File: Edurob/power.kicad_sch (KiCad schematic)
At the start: 26 parts, among them U2 AZ1117-3.3

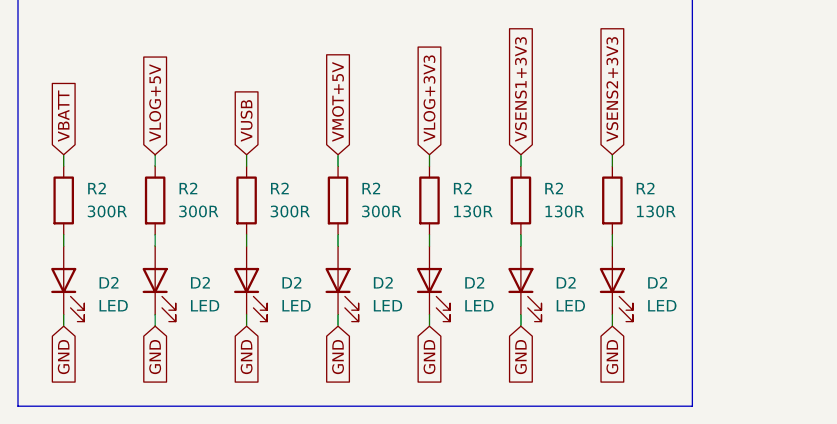
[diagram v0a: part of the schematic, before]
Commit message: Added GPIO Expander, finalized Connector positions
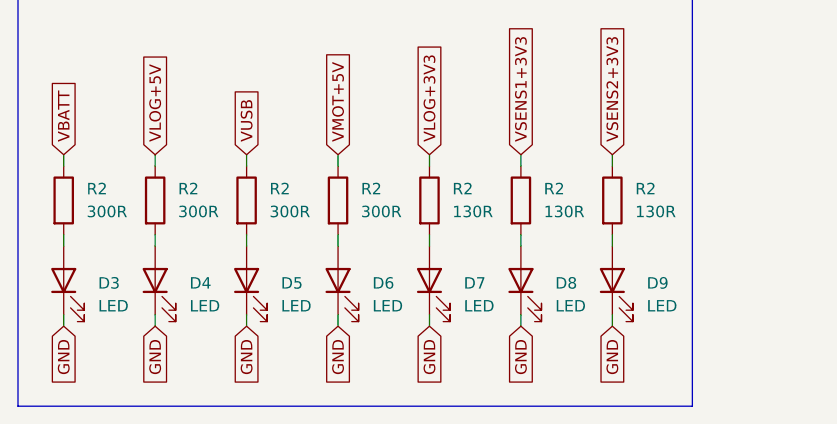
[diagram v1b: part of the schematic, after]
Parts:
- renumbered D2 to D3, D2 to D4, D2 to D5, D2 to D6, D2 to D7, D2 to D8, D2 to D9
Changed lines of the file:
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@@
       )
       (project "Edurob"
-        (path "/ea495553-3cd2-4380-af57-b7ab16ec3dc9"
-          (reference "R1") (unit 1)
-        )
-        (path "/ea495553-3cd2-4380-af57-b7ab16ec3dc9/8aa2f8b0-d8d3-42d6-a936-678d5127e1c2"
-          (reference "R4") (unit 1)
-        )
-        (path "/ea495553-3cd2-4380-af57-b7ab16ec3dc9/172d60ec-c5c3-4534-881f-0378b6cc8d8f"
-          (reference "R6") (unit 1)
-        )
-        (path "/ea495553-3cd2-4380-af57-b7ab16ec3dc9/b565ef5e-ebd0-4632-9832-ca713cd7c533"
-          (reference "R25") (unit 1)
-        )
         (path "/ea495553-3cd2-4380-af57-b7ab16ec3dc9/3d6529d3-09ba-43bd-8600-e24f0f302957"
           (reference "R30") (unit 1)
@@
   (symbol (lib_id "Device:LED") (at 38.1 95.25 90) (unit 1)
     (in_bom yes) (on_board yes) (dnp no) (fields_autoplaced)
-    (property "Reference" "D2" (at 41.91 95.5675 90)
+    (property "Reference" "D5" (at 41.91 95.5675 90)
       (effects (font (size 1.27 1.27)) (justify right))
     )
@@
     (instances
       (project "Edurob"
-        (path "/ea495553-3cd2-4380-af57-b7ab16ec3dc9/b565ef5e-ebd0-4632-9832-ca713cd7c533"
-          (reference "D2") (unit 1)
-        )
         (path "/ea495553-3cd2-4380-af57-b7ab16ec3dc9/3d6529d3-09ba-43bd-8600-e24f0f302957"
           (reference "D5") (unit 1)
@@
   (symbol (lib_id "Device:LED") (at 68.58 95.25 90) (unit 1)
     (in_bom yes) (on_board yes) (dnp no) (fields_autoplaced)
-    (property "Reference" "D2" (at 72.39 95.5675 90)
+    (property "Reference" "D8" (at 72.39 95.5675 90)
       (effects (font (size 1.27 1.27)) (justify right))
     )
@@
     (instances
       (project "Edurob"
-        (path "/ea495553-3cd2-4380-af57-b7ab16ec3dc9/b565ef5e-ebd0-4632-9832-ca713cd7c533"
-          (reference "D2") (unit 1)
-        )
         (path "/ea495553-3cd2-4380-af57-b7ab16ec3dc9/3d6529d3-09ba-43bd-8600-e24f0f302957"
           (reference "D8") (unit 1)
@@
   (symbol (lib_id "Device:LED") (at 58.42 95.25 90) (unit 1)
     (in_bom yes) (on_board yes) (dnp no) (fields_autoplaced)
-    (property "Reference" "D2" (at 62.23 95.5675 90)
+    (property "Reference" "D7" (at 62.23 95.5675 90)
       (effects (font (size 1.27 1.27)) (justify right))
     )
@@
     (instances
       (project "Edurob"
-        (path "/ea495553-3cd2-4380-af57-b7ab16ec3dc9/b565ef5e-ebd0-4632-9832-ca713cd7c533"
-          (reference "D2") (unit 1)
-        )
         (path "/ea495553-3cd2-4380-af57-b7ab16ec3dc9/3d6529d3-09ba-43bd-8600-e24f0f302957"
           (reference "D7") (unit 1)
@@
   (symbol (lib_id "Device:LED") (at 27.94 95.25 90) (unit 1)
     (in_bom yes) (on_board yes) (dnp no) (fields_autoplaced)
-    (property "Reference" "D2" (at 31.75 95.5675 90)
+    (property "Reference" "D4" (at 31.75 95.5675 90)
       (effects (font (size 1.27 1.27)) (justify right))
     )
@@
     (instances
       (project "Edurob"
-        (path "/ea495553-3cd2-4380-af57-b7ab16ec3dc9/b565ef5e-ebd0-4632-9832-ca713cd7c533"
-          (reference "D2") (unit 1)
-        )
         (path "/ea495553-3cd2-4380-af57-b7ab16ec3dc9/3d6529d3-09ba-43bd-8600-e24f0f302957"
           (reference "D4") (unit 1)
@@
       )
       (project "Edurob"
-        (path "/ea495553-3cd2-4380-af57-b7ab16ec3dc9"
-          (reference "R1") (unit 1)
-        )
-        (path "/ea495553-3cd2-4380-af57-b7ab16ec3dc9/8aa2f8b0-d8d3-42d6-a936-678d5127e1c2"
-          (reference "R4") (unit 1)
-        )
-        (path "/ea495553-3cd2-4380-af57-b7ab16ec3dc9/172d60ec-c5c3-4534-881f-0378b6cc8d8f"
-          (reference "R6") (unit 1)
-        )
-        (path "/ea495553-3cd2-4380-af57-b7ab16ec3dc9/b565ef5e-ebd0-4632-9832-ca713cd7c533"
-          (reference "R25") (unit 1)
-        )
         (path "/ea495553-3cd2-4380-af57-b7ab16ec3dc9/3d6529d3-09ba-43bd-8600-e24f0f302957"
           (reference "R29") (unit 1)
@@
       )
       (project "Edurob"
-        (path "/ea495553-3cd2-4380-af57-b7ab16ec3dc9"
-          (reference "R1") (unit 1)
-        )
-        (path "/ea495553-3cd2-4380-af57-b7ab16ec3dc9/8aa2f8b0-d8d3-42d6-a936-678d5127e1c2"
-          (reference "R4") (unit 1)
-        )
-        (path "/ea495553-3cd2-4380-af57-b7ab16ec3dc9/172d60ec-c5c3-4534-881f-0378b6cc8d8f"
-          (reference "R6") (unit 1)
-        )
-        (path "/ea495553-3cd2-4380-af57-b7ab16ec3dc9/b565ef5e-ebd0-4632-9832-ca713cd7c533"
-          (reference "R25") (unit 1)
-        )
         (path "/ea495553-3cd2-4380-af57-b7ab16ec3dc9/3d6529d3-09ba-43bd-8600-e24f0f302957"
           (reference "R31") (unit 1)
@@
       )
       (project "Edurob"
-        (path "/ea495553-3cd2-4380-af57-b7ab16ec3dc9"
-          (reference "R1") (unit 1)
-        )
-        (path "/ea495553-3cd2-4380-af57-b7ab16ec3dc9/8aa2f8b0-d8d3-42d6-a936-678d5127e1c2"
-          (reference "R4") (unit 1)
-        )
-        (path "/ea495553-3cd2-4380-af57-b7ab16ec3dc9/172d60ec-c5c3-4534-881f-0378b6cc8d8f"
-          (reference "R6") (unit 1)
-        )
-        (path "/ea495553-3cd2-4380-af57-b7ab16ec3dc9/b565ef5e-ebd0-4632-9832-ca713cd7c533"
-          (reference "R25") (unit 1)
-        )
         (path "/ea495553-3cd2-4380-af57-b7ab16ec3dc9/3d6529d3-09ba-43bd-8600-e24f0f302957"
           (reference "R26") (unit 1)
@@
       )
       (project "Edurob"
-        (path "/ea495553-3cd2-4380-af57-b7ab16ec3dc9"
-          (reference "R1") (unit 1)
-        )
-        (path "/ea495553-3cd2-4380-af57-b7ab16ec3dc9/8aa2f8b0-d8d3-42d6-a936-678d5127e1c2"
-          (reference "R4") (unit 1)
-        )
-        (path "/ea495553-3cd2-4380-af57-b7ab16ec3dc9/172d60ec-c5c3-4534-881f-0378b6cc8d8f"
-          (reference "R6") (unit 1)
-        )
-        (path "/ea495553-3cd2-4380-af57-b7ab16ec3dc9/b565ef5e-ebd0-4632-9832-ca713cd7c533"
-          (reference "R25") (unit 1)
-        )
         (path "/ea495553-3cd2-4380-af57-b7ab16ec3dc9/3d6529d3-09ba-43bd-8600-e24f0f302957"
           (reference "R28") (unit 1)
@@
   (symbol (lib_id "Device:LED") (at 17.78 95.25 90) (unit 1)
     (in_bom yes) (on_board yes) (dnp no) (fields_autoplaced)
-    (property "Reference" "D2" (at 21.59 95.5675 90)
+    (property "Reference" "D3" (at 21.59 95.5675 90)
       (effects (font (size 1.27 1.27)) (justify right))
     )
@@
     (instances
       (project "Edurob"
-        (path "/ea495553-3cd2-4380-af57-b7ab16ec3dc9/b565ef5e-ebd0-4632-9832-ca713cd7c533"
-          (reference "D2") (unit 1)
-        )
         (path "/ea495553-3cd2-4380-af57-b7ab16ec3dc9/3d6529d3-09ba-43bd-8600-e24f0f302957"
           (reference "D3") (unit 1)
@@
       )
       (project "Edurob"
-        (path "/ea495553-3cd2-4380-af57-b7ab16ec3dc9"
-          (reference "R1") (unit 1)
-        )
-        (path "/ea495553-3cd2-4380-af57-b7ab16ec3dc9/8aa2f8b0-d8d3-42d6-a936-678d5127e1c2"
-          (reference "R4") (unit 1)
-        )
-        (path "/ea495553-3cd2-4380-af57-b7ab16ec3dc9/172d60ec-c5c3-4534-881f-0378b6cc8d8f"
-          (reference "R6") (unit 1)
-        )
-        (path "/ea495553-3cd2-4380-af57-b7ab16ec3dc9/b565ef5e-ebd0-4632-9832-ca713cd7c533"
-          (reference "R25") (unit 1)
-        )
         (path "/ea495553-3cd2-4380-af57-b7ab16ec3dc9/3d6529d3-09ba-43bd-8600-e24f0f302957"
           (reference "R32") (unit 1)
@@
       )
       (project "Edurob"
-        (path "/ea495553-3cd2-4380-af57-b7ab16ec3dc9"
-          (reference "R1") (unit 1)
-        )
-        (path "/ea495553-3cd2-4380-af57-b7ab16ec3dc9/8aa2f8b0-d8d3-42d6-a936-678d5127e1c2"
-          (reference "R4") (unit 1)
-        )
-        (path "/ea495553-3cd2-4380-af57-b7ab16ec3dc9/172d60ec-c5c3-4534-881f-0378b6cc8d8f"
-          (reference "R6") (unit 1)
-        )
-        (path "/ea495553-3cd2-4380-af57-b7ab16ec3dc9/b565ef5e-ebd0-4632-9832-ca713cd7c533"
-          (reference "R25") (unit 1)
-        )
         (path "/ea495553-3cd2-4380-af57-b7ab16ec3dc9/3d6529d3-09ba-43bd-8600-e24f0f302957"
           (reference "R27") (unit 1)
@@
   (symbol (lib_id "Device:LED") (at 78.74 95.25 90) (unit 1)
     (in_bom yes) (on_board yes) (dnp no) (fields_autoplaced)
-    (property "Reference" "D2" (at 82.55 95.5675 90)
+    (property "Reference" "D9" (at 82.55 95.5675 90)
       (effects (font (size 1.27 1.27)) (justify right))
     )
@@
     (instances
       (project "Edurob"
-        (path "/ea495553-3cd2-4380-af57-b7ab16ec3dc9/b565ef5e-ebd0-4632-9832-ca713cd7c533"
-          (reference "D2") (unit 1)
-        )
         (path "/ea495553-3cd2-4380-af57-b7ab16ec3dc9/3d6529d3-09ba-43bd-8600-e24f0f302957"
           (reference "D9") (unit 1)
@@
   (symbol (lib_id "Device:LED") (at 48.26 95.25 90) (unit 1)
     (in_bom yes) (on_board yes) (dnp no) (fields_autoplaced)
-    (property "Reference" "D2" (at 52.07 95.5675 90)
+    (property "Reference" "D6" (at 52.07 95.5675 90)
       (effects (font (size 1.27 1.27)) (justify right))
     )
@@
     (instances
       (project "Edurob"
-        (path "/ea495553-3cd2-4380-af57-b7ab16ec3dc9/b565ef5e-ebd0-4632-9832-ca713cd7c533"
-          (reference "D2") (unit 1)
-        )
         (path "/ea495553-3cd2-4380-af57-b7ab16ec3dc9/3d6529d3-09ba-43bd-8600-e24f0f302957"
           (reference "D6") (unit 1)

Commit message: Release v1.0.1
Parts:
- C5: Manufacturer_Name (none) -> Murata Electronics; Manufacturer_Part_Number (none) -> GRM188R61E106KA73D; Mouser Part Number (none) -> 81-GRM188R61E106KA3D; Mouser Price/Stock (none) -> https://www.mouser.de/ProductDetail/81-GRM188R61E106KA3D; Placed (none) -> True
- C6: Manufacturer_Name (none) -> Murata Electronics; Manufacturer_Part_Number (none) -> ZRB18AR61A226ME01L; Mouser Part Number (none) -> 81-ZRB18AR61A226ME1L; Mouser Price/Stock (none) -> https://www.mouser.de/ProductDetail/Murata-Electronics/ZRB1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; Placed (none) -> True
- D1: Manufacturer_Name (none) -> Diodes Incorporated; Manufacturer_Part_Number (none) -> B340-13-F; Mouser Part Number (none) -> 621-B340-F; Mouser Price/Stock (none) -> https://www.mouser.de/ProductDetail/621-B340-F; Placed (none) -> True
- D3, D4, D5, D6, D7, D8, D9: Manufacturer_Name (none) -> ams OSRAM; Manufacturer_Part_Number (none) -> LO Q976.01-P2R2-25-1; Mouser Part Number (none) -> 720-LOQ976.01P2R2251; Mouser Price/Stock (none) -> https://www.mouser.de/ProductDetail/720-LOQ976.01P2R2251; Placed (none) -> True
- F1, F2: Arrow Part Number 0PTF0078P -> (none); Arrow Price/Stock https://www.arrow.com/en/products/0ptf0078p/littelfuse?regi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 -> (none); Height 11.5 -> (none); Mouser Price/Stock https://www.mouser.co.uk/ProductDetail/Littelfuse/0PTF0078P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 -> https://www.mouser.de/ProductDetail/576-0PTF0078P; Placed (none) -> False
- R2: Manufacturer_Name (none) -> Vishay / Dale; Manufacturer_Part_Number (none) -> CRCW0603130RFKEA; Mouser Part Number (none) -> 71-CRCW0603-130-E3; Mouser Price/Stock (none) -> https://www.mouser.de/ProductDetail/71-CRCW0603-130-E3; Placed (none) -> True
- R2: Manufacturer_Name (none) -> Vishay / Dale; Manufacturer_Part_Number (none) -> CRCW0603300RFKEA; Mouser Part Number (none) -> 71-CRCW0603-300-E3; Mouser Price/Stock (none) -> https://www.mouser.de/ProductDetail/71-CRCW0603-300-E3; Placed (none) -> True
- U2: Manufacturer_Name (none) -> Diodes Incorporated; Manufacturer_Part_Number (none) -> AZ1117CH-3.3TRG1; Mouser Part Number (none) -> 621-AZ1117CH-3.3TRG1; Mouser Price/Stock (none) -> https://www.mouser.de/ProductDetail/621-AZ1117CH-3.3TRG1; Placed (none) -> True
